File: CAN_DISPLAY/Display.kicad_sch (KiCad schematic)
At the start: 16 parts, among them J1 DISPLAY, J14 Display, J16 BME280 Module, J19 TSL2561, J2 I2C Sensor 1, J3 I2C Sensor 2, U6 BME280

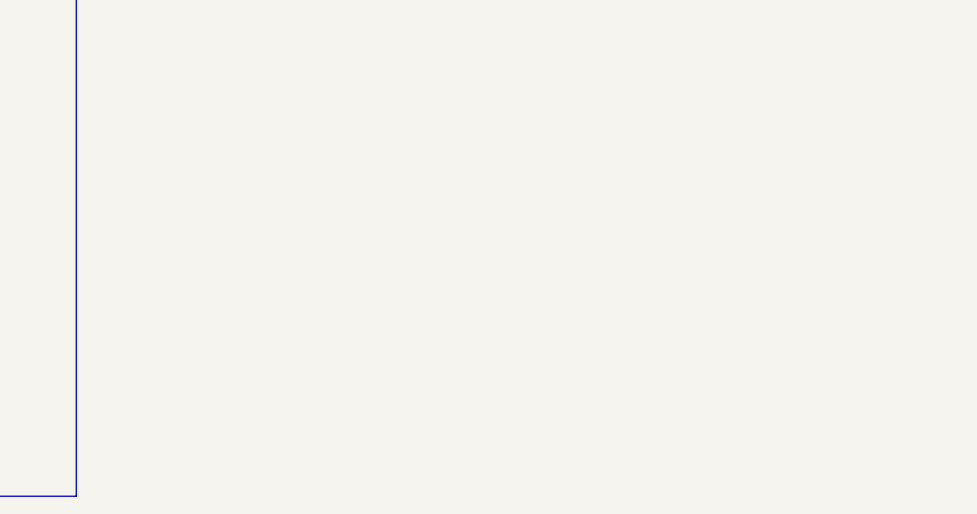
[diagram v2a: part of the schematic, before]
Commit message: Added Light Sensor
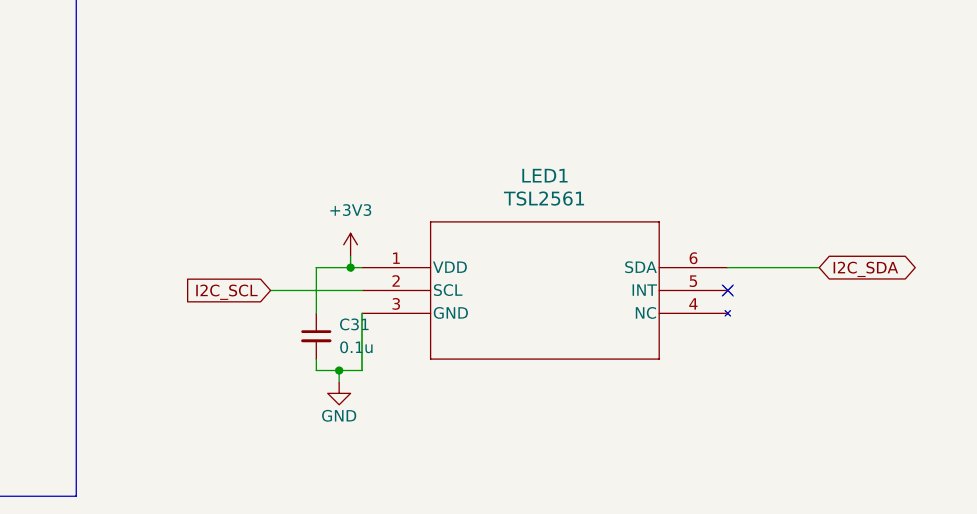
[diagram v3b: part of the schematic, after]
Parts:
- added C31: 0.1u, Capacitor_SMD:C_0805_2012Metric_Pad1.18x1.45mm_HandSolder, symbol Device:C_Small
- added LED1: TSL2561, 1Display:TSL2561, symbol 1Display2:TSL25723FN
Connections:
- net +3V3: now also C31.1, LED1.1 (VDD)
- net GND: now also C31.2, LED1.3 (GND)
- net I2C_SCL: now also LED1.2 (SCL)
- net I2C_SDA: now also LED1.6 (SDA)
- no-connect marks 1 -> 2
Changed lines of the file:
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@@
   (junction (at 54.61 96.52) (diameter 0) (color 0 0 0 0)
   )
+  (junction (at 100.33 167.64) (diameter 0) (color 0 0 0 0)
+  )
   (junction (at 45.085 39.37) (diameter 0) (color 0 0 0 0)
   )
@@
   (junction (at 54.61 127) (diameter 0) (color 0 0 0 0)
   )
+  (junction (at 99.06 179.07) (diameter 0) (color 0 0 0 0)
+  )
   (junction (at 52.07 151.13) (diameter 0) (color 0 0 0 0)
   )
+  (no_connect (at 142.24 170.18))
   (no_connect (at 33.02 44.45))
   (wire (pts (xy 35.56 31.75) (xy 33.02 31.75))
@@
     (stroke (width 0) (type default))
   )
+  (wire (pts (xy 99.06 179.07) (xy 96.52 179.07))
+    (stroke (width 0) (type default))
+  )
   (wire (pts (xy 101.6 95.25) (xy 101.6 93.98))
     (stroke (width 0) (type default))
@@
     (stroke (width 0) (type default))
   )
+  (wire (pts (xy 96.52 179.07) (xy 96.52 177.8))
+    (stroke (width 0) (type default))
+  )
   (wire (pts (xy 92.71 42.545) (xy 92.71 41.275))
     (stroke (width 0) (type default))
@@
     (stroke (width 0) (type default))
   )
+  (wire (pts (xy 101.6 170.18) (xy 91.44 170.18))
+    (stroke (width 0) (type default))
+  )
   (wire (pts (xy 39.37 121.92) (xy 44.45 121.92))
     (stroke (width 0) (type default))
@@
     (stroke (width 0) (type default))
   )
+  (wire (pts (xy 99.06 180.34) (xy 99.06 179.07))
+    (stroke (width 0) (type default))
+  )
   (wire (pts (xy 92.71 34.29) (xy 92.71 36.195))
     (stroke (width 0) (type default))
@@
     (stroke (width 0) (type default))
   )
+  (wire (pts (xy 100.33 166.37) (xy 100.33 167.64))
+    (stroke (width 0) (type default))
+  )
   (wire (pts (xy 39.37 119.38) (xy 39.37 115.57))
     (stroke (width 0) (type default))
@@
     (stroke (width 0) (type default))
   )
+  (wire (pts (xy 96.52 167.64) (xy 100.33 167.64))
+    (stroke (width 0) (type default))
+  )
   (polyline (pts (xy 111.76 61.595) (xy 19.05 61.595))
     (stroke (width 0) (type default))
@@
     (stroke (width 0) (type default))
   )
+  (wire (pts (xy 142.24 167.64) (xy 152.4 167.64))
+    (stroke (width 0) (type default))
+  )
   (wire (pts (xy 52.705 41.91) (xy 46.355 41.91))
     (stroke (width 0) (type default))
@@
     (stroke (width 0) (type default))
   )
+  (wire (pts (xy 101.6 179.07) (xy 99.06 179.07))
+    (stroke (width 0) (type default))
+  )
   (wire (pts (xy 70.485 28.575) (xy 67.945 28.575))
     (stroke (width 0) (type default))
@@
     (stroke (width 0) (type default))
   )
+  (wire (pts (xy 100.33 167.64) (xy 101.6 167.64))
+    (stroke (width 0) (type default))
+  )
   (wire (pts (xy 119.38 118.11) (xy 114.3 118.11))
     (stroke (width 0) (type default))
   )
+  (wire (pts (xy 101.6 172.72) (xy 101.6 179.07))
+    (stroke (width 0) (type default))
+  )
   (wire (pts (xy 39.37 148.59) (xy 36.83 148.59))
     (stroke (width 0) (type default))
@@
   )
   (wire (pts (xy 39.37 115.57) (xy 39.37 114.3))
+    (stroke (width 0) (type default))
+  )
+  (wire (pts (xy 96.52 172.72) (xy 96.52 167.64))
     (stroke (width 0) (type default))
   )
@@
     )
   )
+  (global_label "I2C_SDA" (shape bidirectional) (at 152.4 167.64 0) (fields_autoplaced)
+    (effects (font (size 1.27 1.27)) (justify left))
+    (property "Intersheetrefs" "${INTERSHEET_REFS}" (at 164.1165 167.64 0)
+      (effects (font (size 1.27 1.27)) (justify left) hide)
+    )
+  )
   (global_label "RX_DISPLAY_TX" (shape output) (at 61.595 41.91 0) (fields_autoplaced)
     (effects (font (size 1.27 1.27)) (justify left))
@@
     )
   )
+  (global_label "I2C_SCL" (shape input) (at 91.44 170.18 180) (fields_autoplaced)
+    (effects (font (size 1.27 1.27)) (justify right))
+    (property "Intersheetrefs" "${INTERSHEET_REFS}" (at 80.8953 170.18 0)
+      (effects (font (size 1.27 1.27)) (justify right) hide)
+    )
+  )
   (global_label "I2C_SDA" (shape bidirectional) (at 56.515 96.52 0) (fields_autoplaced)
     (effects (font (size 1.27 1.27)) (justify left))
@@
         (path "/7b7bcc60-3b35-483b-8f75-db7ec854d7bb/ea039cf5-2d2d-4347-8210-9e077b57066c"
           (reference "#PWR086") (unit 1)
+        )
+      )
+    )
+  )
+  (symbol (lib_id "1Display2:TSL25723FN") (at 101.6 167.64 0) (unit 1)
+    (in_bom yes) (on_board yes) (dnp no) (fields_autoplaced)
+    (property "Reference" "LED1" (at 121.92 157.48 0)
+      (effects (font (size 1.524 1.524)))
+    )
+    (property "Value" "TSL2561" (at 121.92 160.02 0)
+      (effects (font (size 1.524 1.524)))
+    )
+    (property "Footprint" "1Display:TSL2561" (at 101.6 167.64 0)
+      (effects (font (size 1.27 1.27) italic) hide)
+    )
+    (property "Datasheet" "TSL25723FN" (at 101.6 167.64 0)
+      (effects (font (size 1.27 1.27) italic) hide)
+    )
+    (pin "1")
+    (pin "2")
+    (pin "3")
+    (pin "4")
+    (pin "5")
+    (pin "6")
+    (instances
+      (project "CAN_DISPLAY"
+        (path "/7b7bcc60-3b35-483b-8f75-db7ec854d7bb/ea039cf5-2d2d-4347-8210-9e077b57066c"
+          (reference "LED1") (unit 1)
         )
       )
@@
     )
   )
+  (symbol (lib_id "Device:C_Small") (at 96.52 175.26 0) (unit 1)
+    (in_bom yes) (on_board yes) (dnp no) (fields_autoplaced)
+    (property "Reference" "C31" (at 99.06 173.9963 0)
+      (effects (font (size 1.27 1.27)) (justify left))
+    )
+    (property "Value" "0.1u" (at 99.06 176.5363 0)
+      (effects (font (size 1.27 1.27)) (justify left))
+    )
+    (property "Footprint" "Capacitor_SMD:C_0805_2012Metric_Pad1.18x1.45mm_HandSolder" (at 96.52 175.26 0)
+      (effects (font (size 1.27 1.27)) hide)
+    )
+    (property "Datasheet" "~" (at 96.52 175.26 0)
+      (effects (font (size 1.27 1.27)) hide)
+    )
+    (pin "1")
+    (pin "2")
+    (instances
+      (project "CAN_DISPLAY"
+        (path "/7b7bcc60-3b35-483b-8f75-db7ec854d7bb/ea039cf5-2d2d-4347-8210-9e077b57066c"
+          (reference "C31") (unit 1)
+        )
+      )
+    )
+  )
   (symbol (lib_id "Jumper:SolderJumper_3_Bridged12") (at 139.065 102.87 270) (unit 1)
     (in_bom yes) (on_board yes) (dnp no)
@@
         )
       )
+    )
+  )
+  (symbol (lib_id "power:+3V3") (at 100.33 166.37 0) (unit 1)
+    (in_bom yes) (on_board yes) (dnp no) (fields_autoplaced)
+    (property "Reference" "#PWR093" (at 100.33 170.18 0)
+      (effects (font (size 1.27 1.27)) hide)
+    )
+    (property "Value" "+3V3" (at 100.33 161.29 0)
+      (effects (font (size 1.27 1.27)))
+    )
+    (property "Footprint" "" (at 100.33 166.37 0)
+      (effects (font (size 1.27 1.27)) hide)
+    )
+    (property "Datasheet" "" (at 100.33 166.37 0)
+      (effects (font (size 1.27 1.27)) hide)
+    )
+    (pin "1")
+    (instances
+      (project "CAN_DISPLAY"
+        (path "/7b7bcc60-3b35-483b-8f75-db7ec854d7bb/ea039cf5-2d2d-4347-8210-9e077b57066c"
+          (reference "#PWR093") (unit 1)
+        )
+      )
+    )
+  )
+  (symbol (lib_id "power:GND") (at 99.06 180.34 0) (mirror y) (unit 1)
+    (in_bom yes) (on_board yes) (dnp no)
+    (property "Reference" "#PWR094" (at 99.06 186.69 0)
+      (effects (font (size 1.27 1.27)) hide)
+    )
+    (property "Value" "GND" (at 99.06 184.15 0)
+      (effects (font (size 1.27 1.27)))
+    )
+    (property "Footprint" "" (at 99.06 180.34 0)
+      (effects (font (size 1.27 1.27)) hide)
+    )
+    (property "Datasheet" "" (at 99.06 180.34 0)
+      (effects (font (size 1.27 1.27)) hide)
+    )
+    (pin "1")
+    (instances
+      (project "CAN_DISPLAY"
+        (path "/7b7bcc60-3b35-483b-8f75-db7ec854d7bb/ea039cf5-2d2d-4347-8210-9e077b57066c"
+          (reference "#PWR094") (unit 1)
+        )
+      )

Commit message: Add SW
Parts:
- added BZ1: Buzzer, Buzzer_Beeper:Buzzer_12x9.5RM7.6, symbol Device:Buzzer
- added D6: 1N4007, Diode_THT:D_DO-41_SOD81_P10.16mm_Horizontal, symbol Diode:1N4007
- added Q1: BC547, Package_TO_SOT_SMD:SOT-23, symbol Transistor_BJT:BC547
- added R2: 1K, Resistor_SMD:R_0805_2012Metric_Pad1.20x1.40mm_HandSolder, symbol Device:R_Small
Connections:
- net +5V: now also BZ1.1 (-), D6.1 (K)
- net GND: now also Q1.3 (E)
- new net: BZ1.2 (+), D6.2 (A), Q1.1 (C)
- new net: Q1.2 (B), R2.1
- new net BUZZER: R2.2
